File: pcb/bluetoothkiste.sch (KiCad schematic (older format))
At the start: 17 parts, among them J1 DB9_Female, J2 Screw_Terminal_01x03, J3 Screw_Terminal_01x03, J4 RJ45, J5 USB_A, J6 Conn_01x04_Female, J7 Screw_Terminal_01x03, U1 L7805, U2 MAX232

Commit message: beschriftungen pcb
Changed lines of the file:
@@
 Wire Wire Line
 	3550 7050 2950 7050
+Text Label 2950 6850 0    50   ~ 0
+COMMON-RX
+Text Label 2950 6750 0    50   ~ 0
+COMMON-TX
+Text Label 2950 6550 0    50   ~ 0
+FLARM-TX
+Text Label 2950 7050 0    50   ~ 0
+FLARM-RX
 Text Label 2950 6650 0    50   ~ 0
-COMMON-RX
-Text Label 2950 6550 0    50   ~ 0
-COMMON-TX
-Text Label 2950 6750 0    50   ~ 0
-FLARM-TX
-Text Label 2950 6850 0    50   ~ 0
-FLARM-RX
+LX-TX
 Text Label 2950 6950 0    50   ~ 0
-LX-TX
-Text Label 2950 7050 0    50   ~ 0
 LX-RX
 Wire Wire Line

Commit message: dual channel
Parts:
- removed J3, J7: Screw_Terminal_01x03, TerminalBlock_MetzConnect:TerminalBlock_MetzConnect_Type059_RT06303HBWC_1x03_P3.50mm_Horizontal, symbol Connector:Screw_Terminal_01x03
- removed J5: USB_A, JS_Local:USB_A_UPRIGHT_SEGOR, symbol Connector:USB_A
- added J3: Conn_01x04_Female, Connector_PinSocket_2.54mm:PinSocket_1x04_P2.54mm_Horizontal, symbol Connector:Conn_01x04_Female
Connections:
- net labels added: FLARM-BT-RX, FLARM-BT-TX, LX-BT-RX, LX-BT-TX
- net labels removed: BT-RX, BT-TX, COMMON-RX, COMMON-TX
- wire segments 74 -> 68
- no-connect marks 11 -> 7
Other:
- note added: "+12P = Geschaltete 12V, um die Bluetooth-Module\nausschalten zu können"
- note added: "HC-06 (FLARM)"
- note added: "HC-06 (LX)"
- note removed: "+12P = Geschaltete 12V, um das Bluetooth-Modul \nausschalten zu können"
- note removed: "COMMON-TX sollte über einen Umschalter mit\nFLARM-TX bzw. LX-TX verbunden werden, \num zwischen Flarm und LX wählen zu können. \nGenauso COMMON-RX mit FLARM-/LX-RX."
- note removed: "HC-06"
- moved on the sheet: J6
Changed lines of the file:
@@
 L Connector:Conn_01x04_Female J6
 U 1 1 5C93D289
-P 7450 4950
-F 0 "J6" H 7400 5300 50  0000 L CNN
-F 1 "Conn_01x04_Female" H 7100 5200 50  0000 L CNN
-F 2 "Connector_PinSocket_2.54mm:PinSocket_1x04_P2.54mm_Horizontal" H 7450 4950 50  0001 C CNN
-F 3 "~" H 7450 4950 50  0001 C CNN
-	1    7450 4950
+P 6750 3150
+F 0 "J6" H 6700 3500 50  0000 L CNN
+F 1 "Conn_01x04_Female" H 6400 3400 50  0000 L CNN
+F 2 "Connector_PinSocket_2.54mm:PinSocket_1x04_P2.54mm_Horizontal" H 6750 3150 50  0001 C CNN
+F 3 "~" H 6750 3150 50  0001 C CNN
+	1    6750 3150
 	-1   0    0    1
 $EndComp
@@
 $EndComp
 Connection ~ 4850 4300
-Text Notes 7250 4775 0    50   ~ 0
+Text Notes 6550 2975 0    50   ~ 0
 VCC
-Text Notes 7250 4875 0    50   ~ 0
+Text Notes 6550 3075 0    50   ~ 0
 GND
-Text Notes 7250 4975 0    50   ~ 0
+Text Notes 6550 3175 0    50   ~ 0
 TX
-Text Notes 7250 5075 0    50   ~ 0
+Text Notes 6550 3275 0    50   ~ 0
 RX
-Text Notes 7150 4650 0    50   ~ 0
-HC-06
+Text Notes 6450 2850 0    50   ~ 0
+HC-06 (FLARM)
 Wire Wire Line
 	1700 5300 1400 5300
@@
 NoConn ~ 1700 5200
 Wire Wire Line
-	3550 6550 2950 6550
-Wire Wire Line
-	3550 6650 2950 6650
-Wire Wire Line
-	3550 6750 2950 6750
-Wire Wire Line
-	3550 6850 2950 6850
-Wire Wire Line
-	3550 6950 2950 6950
-Wire Wire Line
-	3550 7050 2950 7050
-Text Label 2950 6850 0    50   ~ 0
-COMMON-RX
-Text Label 2950 6750 0    50   ~ 0
-COMMON-TX
-Text Label 2950 6550 0    50   ~ 0
-FLARM-TX
-Text Label 2950 7050 0    50   ~ 0
-FLARM-RX
-Text Label 2950 6650 0    50   ~ 0
-LX-TX
-Text Label 2950 6950 0    50   ~ 0
-LX-RX
-Wire Wire Line
 	3550 5900 3250 5900
 Wire Wire Line
@@
 $EndComp
 Text Notes 2950 6350 0    50   ~ 0
-+12P = Geschaltete 12V, um das Bluetooth-Modul \nausschalten zu können
-Text Notes 2950 7500 0    50   ~ 0
-COMMON-TX sollte über einen Umschalter mit\nFLARM-TX bzw. LX-TX verbunden werden, \num zwischen Flarm und LX wählen zu können. \nGenauso COMMON-RX mit FLARM-/LX-RX.
++12P = Geschaltete 12V, um die Bluetooth-Module\nausschalten zu können
 $Comp
 L Interface_UART:MAX232 U2
@@
 	3400 5500 4850 5500
 Wire Wire Line
-	8100 5500 8100 6200
-Wire Wire Line
-	8100 6200 9550 6200
-Wire Wire Line
 	9550 6200 9550 6100
 Wire Wire Line
@@
 Wire Wire Line
 	1400 5500 3400 5500
-Text Label 10350 5000 0    50   ~ 0
-COMMON-RX
-Text Label 10350 5400 0    50   ~ 0
-COMMON-TX
-Wire Wire Line
-	8750 5000 8350 5000
-Wire Wire Line
-	8750 5400 8350 5400
-Text Label 8350 5400 0    50   ~ 0
-BT-RX
-Text Label 8350 5000 0    50   ~ 0
-BT-TX
-Wire Wire Line
-	7650 5050 7900 5050
-Wire Wire Line
-	7650 4950 7900 4950
-Text Label 7700 4950 0    50   ~ 0
-BT-TX
-Text Label 7700 5050 0    50   ~ 0
-BT-RX
+Text Label 8150 5400 0    50   ~ 0
+LX-BT-RX
+Text Label 8150 5000 0    50   ~ 0
+LX-BT-TX
+Text Label 7100 3250 0    50   ~ 0
+FLARM-BT-RX
 Connection ~ 9550 6200
 $Comp
@@
 Wire Wire Line
 	10950 4800 10950 6200
-NoConn ~ 10350 5200
-NoConn ~ 10350 5600
-NoConn ~ 8750 5600
-NoConn ~ 8750 5200
 $Comp
 L Device:C C7
@@
 Wire Wire Line
 	9550 3700 9550 3600
-$Comp
-L Connector:USB_A J5
-U 1 1 5CA5D0AD
-P 6350 4900
-F 0 "J5" H 6407 5367 50  0000 C CNN
-F 1 "USB_A" H 6407 5276 50  0000 C CNN
-F 2 "JS_Local:USB_A_UPRIGHT_SEGOR" H 6500 4850 50  0001 C CNN
-F 3 " ~" H 6500 4850 50  0001 C CNN
-	1    6350 4900
-	1    0    0    -1
-$EndComp
-Wire Wire Line
-	6250 5300 6250 5400
-Wire Wire Line
-	6250 5400 6350 5400
-Wire Wire Line
-	6650 4700 6750 4700
-Wire Wire Line
-	6750 4700 6750 4300
-Wire Wire Line
-	6350 5300 6350 5400
-Connection ~ 6350 5400
-Wire Wire Line
-	6350 5400 6350 5500
 Wire Wire Line
 	10650 4500 10950 4500
@@
 	9550 3600 10950 3600
 Wire Wire Line
-	7250 5800 7250 6450
-Wire Wire Line
 	5400 5500 5800 5500
 Wire Wire Line
@@
 Text Notes 5300 4000 0    50   ~ 0
 R-785.0-1.0 Schaltregler\n5V 1A
-Text Label 6650 5000 0    50   ~ 0
-COMMON-TX
-Text Label 6650 4900 0    50   ~ 0
-COMMON-RX
-Connection ~ 6350 5500
-Connection ~ 6750 4300
 Connection ~ 5800 4300
 Connection ~ 5800 5500
-Wire Wire Line
-	5800 5500 6350 5500
-Wire Wire Line
-	5800 4300 6750 4300
 $Comp
 L power:+12P #PWR0110
@@
 Wire Wire Line
 	4850 3900 4850 3850
-Wire Wire Line
-	6350 5500 8100 5500
-Wire Wire Line
-	6750 4300 8100 4300
-Wire Wire Line
-	7650 4750 8100 4750
-Wire Wire Line
-	8100 4750 8100 4300
-Connection ~ 8100 4300
-Wire Wire Line
-	7650 4850 8100 4850
-Wire Wire Line
-	8100 4850 8100 5500
-Connection ~ 8100 5500
-$Comp
-L Connector:Screw_Terminal_01x03 J3
-U 1 1 5CF44711
-P 3750 6650
-F 0 "J3" H 3850 6700 50  0000 L CNN
-F 1 "Screw_Terminal_01x03" H 3850 6600 50  0000 L CNN
-F 2 "TerminalBlock_MetzConnect:TerminalBlock_MetzConnect_Type059_RT06303HBWC_1x03_P3.50mm_Horizontal" H 3750 6650 50  0001 C CNN
-F 3 "~" H 3750 6650 50  0001 C CNN
-	1    3750 6650
-	1    0    0    -1
-$EndComp
-$Comp
-L Connector:Screw_Terminal_01x03 J7
-U 1 1 5CF44F19
-P 3750 6950
-F 0 "J7" H 3850 7000 50  0000 L CNN
-F 1 "Screw_Terminal_01x03" H 3850 6900 50  0000 L CNN
-F 2 "TerminalBlock_MetzConnect:TerminalBlock_MetzConnect_Type059_RT06303HBWC_1x03_P3.50mm_Horizontal" H 3750 6950 50  0001 C CNN
-F 3 "~" H 3750 6950 50  0001 C CNN
-	1    3750 6950
-	1    0    0    -1
-$EndComp
+$Comp
+L Connector:Conn_01x04_Female J3
+U 1 1 5D01F109
+P 6750 2250
+F 0 "J3" H 6700 2600 50  0000 L CNN
+F 1 "Conn_01x04_Female" H 6400 2500 50  0000 L CNN
+F 2 "Connector_PinSocket_2.54mm:PinSocket_1x04_P2.54mm_Horizontal" H 6750 2250 50  0001 C CNN
+F 3 "~" H 6750 2250 50  0001 C CNN
+	1    6750 2250
+	-1   0    0    1
+$EndComp
+Text Notes 6550 2075 0    50   ~ 0
+VCC
+Text Notes 6550 2175 0    50   ~ 0
+GND
+Text Notes 6550 2275 0    50   ~ 0
+TX
+Text Notes 6550 2375 0    50   ~ 0
+RX
+Text Notes 6450 1950 0    50   ~ 0
+HC-06 (LX)
+Text Label 7100 3150 0    50   ~ 0
+FLARM-BT-TX
+Wire Wire Line
+	6950 3150 7100 3150
+Wire Wire Line
+	6950 3250 7100 3250
+Wire Wire Line
+	6950 2350 7100 2350
+Wire Wire Line
+	6950 2250 7100 2250
+Text Label 7100 2250 0    50   ~ 0
+LX-BT-TX
+Text Label 7100 2350 0    50   ~ 0
+LX-BT-RX
+Wire Wire Line
+	6950 2050 7900 2050
+Wire Wire Line
+	7900 2050 7900 2950
+Connection ~ 7900 4300
+Wire Wire Line
+	7900 4300 8100 4300
+Connection ~ 7900 2950
+Wire Wire Line
+	7900 2950 7900 4300
+Wire Wire Line
+	6950 3050 7800 3050
+Wire Wire Line
+	7800 2150 6950 2150
+Wire Wire Line
+	6950 2950 7900 2950
+Wire Wire Line
+	7800 2150 7800 3050
+Wire Wire Line
+	7800 3050 7800 5500
+Connection ~ 7800 3050
+Wire Wire Line
+	7800 5500 7800 6200
+Wire Wire Line
+	7800 6200 9550 6200
+Connection ~ 7800 5500
+Wire Wire Line
+	8150 5400 8750 5400
+Wire Wire Line
+	8150 5000 8750 5000
+Wire Wire Line
+	8750 5200 8150 5200
+Wire Wire Line
+	8150 5600 8750 5600
+Text Label 8150 5200 0    50   ~ 0
+FLARM-BT-TX
+Text Label 8150 5600 0    50   ~ 0
+FLARM-BT-RX
+Text Label 10350 5400 0    50   ~ 0
+LX-TX
+Text Label 10350 5600 0    50   ~ 0
+FLARM-TX
+Text Label 10350 5200 0    50   ~ 0
+FLARM-RX
+Text Label 10350 5000 0    50   ~ 0
+LX-RX
+Wire Wire Line
+	5800 4300 7900 4300
+Wire Wire Line
+	5800 5500 7800 5500
 $EndSCHEMATC

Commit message: bugs in schematic
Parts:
- added J5: USB_A, symbol Connector:USB_A
- added JP1: Jumper, symbol Device:Jumper
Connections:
- net +12P: now also JP1.2
- net +12V: now also J4.7, J4.8, JP1.1; no longer J4.1, J4.2
- net +5V: now also J5.1 (VBUS)
- net FLARM-RX: now also J4.3; no longer J4.6
- net FLARM-TX: now also J4.4; no longer J4.5
- net GND: now also J4.1, J4.2, J4.5, J5.4 (GND), J5.5 (Shield); no longer J4.4, J4.7, J4.8
- net LX-RX: now also J1.3; no longer J1.2
- net LX-TX: now also J1.2; no longer J1.3
- no-connect marks 7 -> 9
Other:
- note added: "+12P = Stromversorgung Bluetooth-Module (intern abgesichert)\n+12V = Stromversorgung FLARM (intern nicht abgesichert)"
- note added: "Jumper zum Verbinden der Stromversorgung \nder Bluetooth-Module und des FLARM. \nFalls man nicht getrennt ein- und ausschalten\nmöchte kann man diesen Jumper setzen."
- note removed: "+12P = Geschaltete 12V, um die Bluetooth-Module\nausschalten zu können"
- moved on the sheet: J4
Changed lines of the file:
@@
 L Connector:RJ45 J4
 U 1 1 5C93DA28
-P 4100 4850
-F 0 "J4" H 3770 4854 50  0000 R CNN
-F 1 "RJ45" H 3770 4945 50  0000 R CNN
-F 2 "JS_Local:RJ45_SEGOR" V 4100 4875 50  0001 C CNN
-F 3 "~" V 4100 4875 50  0001 C CNN
-	1    4100 4850
-	-1   0    0    1
+P 3300 4950
+F 0 "J4" H 2970 4954 50  0000 R CNN
+F 1 "RJ45" H 2970 5045 50  0000 R CNN
+F 2 "JS_Local:RJ45_SEGOR" V 3300 4975 50  0001 C CNN
+F 3 "~" V 3300 4975 50  0001 C CNN
+	1    3300 4950
+	1    0    0    -1
 $EndComp
 $Comp
@@
 	1700 5300 1400 5300
 Wire Wire Line
-	3700 5250 3400 5250
-Wire Wire Line
-	3700 5150 3400 5150
-Wire Wire Line
-	3400 5150 3400 5250
-Wire Wire Line
-	3700 4850 3400 4850
-Wire Wire Line
-	3400 4850 3400 5150
-Connection ~ 3400 5150
+	3900 5150 3900 5250
+Wire Wire Line
+	3900 4850 3900 5150
+Connection ~ 3900 5150
 NoConn ~ 3700 4750
-Wire Wire Line
-	3700 4650 3600 4650
-Wire Wire Line
-	3700 4550 3600 4550
-Wire Wire Line
-	3600 4550 3600 4650
-Connection ~ 3600 4650
-Wire Wire Line
-	3600 4650 3400 4650
-Wire Wire Line
-	3700 4950 2750 4950
-Text Label 2750 4950 0    50   ~ 0
+Text Label 4150 4950 0    50   ~ 0
 FLARM-TX
-Wire Wire Line
-	3700 5050 2750 5050
-Text Label 2750 5050 0    50   ~ 0
+Text Label 4150 5050 0    50   ~ 0
 FLARM-RX
 Wire Wire Line
 	750  4900 1700 4900
-Text Label 750  4900 0    50   ~ 0
+Text Label 750  4700 0    50   ~ 0
 LX-TX
 NoConn ~ 1700 4500
@@
 $EndComp
 Text Notes 2950 6350 0    50   ~ 0
-+12P = Geschaltete 12V, um die Bluetooth-Module\nausschalten zu können
++12P = Stromversorgung Bluetooth-Module (intern abgesichert)\n+12V = Stromversorgung FLARM (intern nicht abgesichert)
 $Comp
 L Interface_UART:MAX232 U2
@@
 	4850 5500 5400 5500
 Wire Wire Line
-	3400 5250 3400 5500
-Connection ~ 3400 5250
-Connection ~ 3400 5500
-Wire Wire Line
-	3400 5500 4850 5500
+	3900 5250 3900 5500
+Connection ~ 3900 5250
 Wire Wire Line
 	9550 6200 9550 6100
@@
 $EndComp
 Wire Wire Line
-	4550 4300 3400 4300
-Wire Wire Line
-	3400 4650 3400 4300
-Connection ~ 3400 4300
-Wire Wire Line
-	3400 4300 750  4300
+	4550 4300 3900 4300
+Wire Wire Line
+	3900 4650 3900 4550
 $Comp
 L power:+12V #PWR0106
 U 1 1 5CA1F7A5
-P 4550 4300
-F 0 "#PWR0106" H 4550 4150 50  0001 C CNN
-F 1 "+12V" H 4565 4473 50  0000 C CNN
-F 2 "" H 4550 4300 50  0001 C CNN
-F 3 "" H 4550 4300 50  0001 C CNN
-	1    4550 4300
+P 4400 2300
+F 0 "#PWR0106" H 4400 2150 50  0001 C CNN
+F 1 "+12V" H 4415 2473 50  0000 C CNN
+F 2 "" H 4400 2300 50  0001 C CNN
+F 3 "" H 4400 2300 50  0001 C CNN
+	1    4400 2300
 	1    0    0    -1
 $EndComp
@@
 	1    0    0    -1
 $EndComp
-Text Label 750  4700 0    50   ~ 0
+Text Label 750  4900 0    50   ~ 0
 LX-RX
 Wire Wire Line
@@
 	1400 5300 1400 5500
 Connection ~ 1400 5500
-Wire Wire Line
-	1400 5500 3400 5500
 Text Label 8150 5400 0    50   ~ 0
 LX-BT-RX
@@
 L power:+12P #PWR0110
 U 1 1 5C941CC9
-P 4850 3850
-F 0 "#PWR0110" H 4850 3700 50  0001 C CNN
-F 1 "+12P" H 4865 4023 50  0000 C CNN
-F 2 "" H 4850 3850 50  0001 C CNN
-F 3 "" H 4850 3850 50  0001 C CNN
-	1    4850 3850
+P 5000 2300
+F 0 "#PWR0110" H 5000 2150 50  0001 C CNN
+F 1 "+12P" H 5015 2473 50  0000 C CNN
+F 2 "" H 5000 2300 50  0001 C CNN
+F 3 "" H 5000 2300 50  0001 C CNN
+	1    5000 2300
 	1    0    0    -1
 $EndComp
@@
 Wire Wire Line
 	4850 4200 4850 4300
-Wire Wire Line
-	4850 3900 4850 3850
 $Comp
 L Connector:Conn_01x04_Female J3
@@
 LX-RX
 Wire Wire Line
-	5800 4300 7900 4300
-Wire Wire Line
-	5800 5500 7800 5500
+	5800 4300 7250 4300
+Wire Wire Line
+	5800 5500 6600 5500
+$Comp
+L Connector:USB_A J5
+U 1 1 5D2F7C66
+P 6700 4850
+F 0 "J5" H 6757 5317 50  0000 C CNN
+F 1 "USB_A" H 6757 5226 50  0000 C CNN
+F 2 "" H 6850 4800 50  0001 C CNN
+F 3 " ~" H 6850 4800 50  0001 C CNN
+	1    6700 4850
+	1    0    0    -1
+$EndComp
+NoConn ~ 7000 4850
+NoConn ~ 7000 4950
+Wire Wire Line
+	7000 4650 7250 4650
+Wire Wire Line
+	7250 4650 7250 4300
+Connection ~ 7250 4300
+Wire Wire Line
+	7250 4300 7900 4300
+Wire Wire Line
+	6700 5250 6700 5500
+Connection ~ 6700 5500
+Wire Wire Line
+	6700 5500 7800 5500
+Wire Wire Line
+	6600 5250 6600 5500
+Connection ~ 6600 5500
+Wire Wire Line
+	6600 5500 6700 5500
+Connection ~ 3900 5500
+Wire Wire Line
+	3900 5500 4850 5500
+Wire Wire Line
+	1400 5500 3900 5500
+Connection ~ 3900 4300
+Wire Wire Line
+	750  4300 3900 4300
+Wire Wire Line
+	3900 5150 3700 5150
+Wire Wire Line
+	3700 5250 3900 5250
+Wire Wire Line
+	3900 4850 3700 4850
+Wire Wire Line
+	3900 4650 3700 4650
+Wire Wire Line
+	3700 4550 3900 4550
+Connection ~ 3900 4550
+Wire Wire Line
+	3900 4550 3900 4300
+Wire Wire Line
+	3700 4950 4150 4950
+Wire Wire Line
+	3700 5050 4150 5050
+$Comp
+L Device:Jumper JP1
+U 1 1 5D378146
+P 4700 2700
+F 0 "JP1" H 4700 2964 50  0000 C CNN
+F 1 "Jumper" H 4700 2873 50  0000 C CNN
+F 2 "" H 4700 2700 50  0001 C CNN
+F 3 "~" H 4700 2700 50  0001 C CNN
+	1    4700 2700
+	1    0    0    -1
+$EndComp
+Wire Wire Line
+	5000 2700 5000 3400
+Wire Wire Line
+	5000 3400 4850 3400
+Wire Wire Line
+	4400 2300 4400 2700
+Wire Wire Line
+	4850 3400 4850 3900
+Wire Wire Line
+	5000 2700 5000 2300
+Connection ~ 5000 2700
+Wire Wire Line
+	4400 2700 4400 3400
+Wire Wire Line
+	4400 3400 4550 3400
+Wire Wire Line
+	4550 3400 4550 4300
+Connection ~ 4400 2700
+Text Notes 2450 2900 0    50   ~ 0
+Jumper zum Verbinden der  Stromversorgung \nder Bluetooth-Module und des FLARM. \nFalls man nicht getrennt ein- und ausschalten\nmöchte kann man diesen Jumper setzen.
 $EndSCHEMATC

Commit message: layout updated
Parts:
- J2: footprint TerminalBlock_MetzConnect:TerminalBlock_MetzConnect_Type059_RT06303HBWC_1x03_P3.50mm_Horizontal -> TerminalBlock_MetzConnect:TerminalBlock_MetzConnect_Type055_RT01503HDWU_1x03_P5.00mm_Horizontal
- J5: footprint (none) -> JS_Local:USB_A_UPRIGHT_SEGOR
- JP1: footprint (none) -> Connector_PinHeader_2.54mm:PinHeader_1x02_P2.54mm_Vertical
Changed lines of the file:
@@
 F 0 "J2" H 3850 6050 50  0000 L CNN
 F 1 "Screw_Terminal_01x03" H 3850 5950 50  0000 L CNN
-F 2 "TerminalBlock_MetzConnect:TerminalBlock_MetzConnect_Type059_RT06303HBWC_1x03_P3.50mm_Horizontal" H 3750 6000 50  0001 C CNN
+F 2 "TerminalBlock_MetzConnect:TerminalBlock_MetzConnect_Type055_RT01503HDWU_1x03_P5.00mm_Horizontal" H 3750 6000 50  0001 C CNN
 F 3 "~" H 3750 6000 50  0001 C CNN
 	1    3750 6000
@@
 F 0 "J5" H 6757 5317 50  0000 C CNN
 F 1 "USB_A" H 6757 5226 50  0000 C CNN
-F 2 "" H 6850 4800 50  0001 C CNN
+F 2 "JS_Local:USB_A_UPRIGHT_SEGOR" H 6850 4800 50  0001 C CNN
 F 3 " ~" H 6850 4800 50  0001 C CNN
 	1    6700 4850
@@
 F 0 "JP1" H 4700 2964 50  0000 C CNN
 F 1 "Jumper" H 4700 2873 50  0000 C CNN
-F 2 "" H 4700 2700 50  0001 C CNN
+F 2 "Connector_PinHeader_2.54mm:PinHeader_1x02_P2.54mm_Vertical" H 4700 2700 50  0001 C CNN
 F 3 "~" H 4700 2700 50  0001 C CNN
 	1    4700 2700

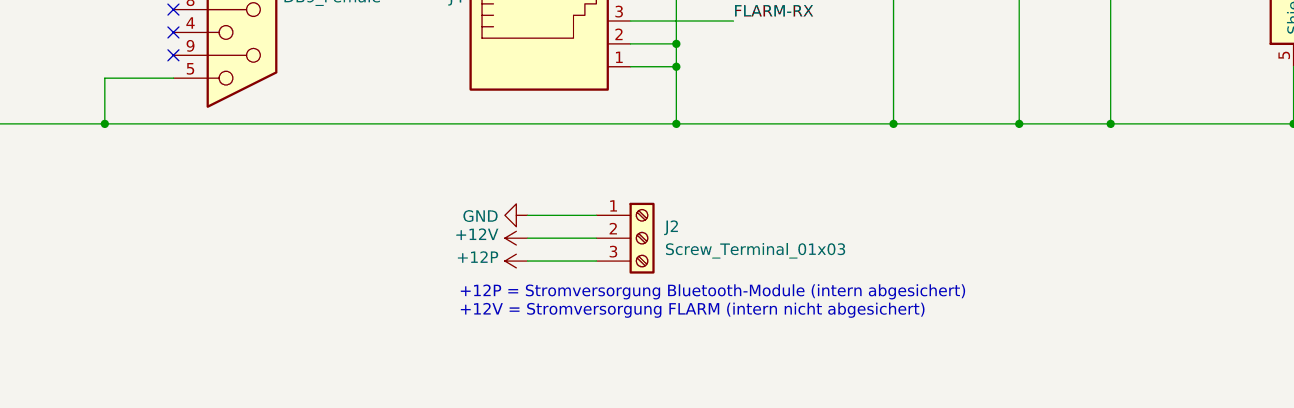
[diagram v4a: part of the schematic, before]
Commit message: dioden verpolungsschutz
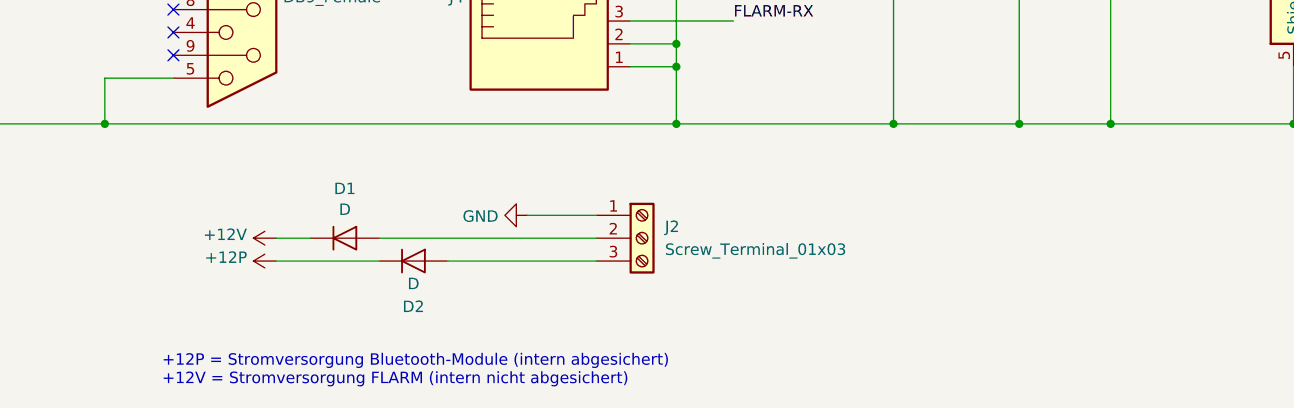
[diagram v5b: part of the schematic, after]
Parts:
- added D1, D2: D, Diode_THT:D_A-405_P7.62mm_Horizontal, symbol Device:D
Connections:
- net +12P: now also D2.1 (K); no longer J2.3 (Pin_3)
- net +12V: now also D1.1 (K); no longer J2.2 (Pin_2)
- new net: D1.2 (A), J2.2 (Pin_2)
- new net: D2.2 (A), J2.3 (Pin_3)
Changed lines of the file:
@@
 Wire Wire Line
 	3550 5900 3250 5900
-Wire Wire Line
-	3550 6000 3250 6000
-Wire Wire Line
-	3550 6100 3250 6100
 $Comp
 L power:GND #PWR0102
@@
 L power:+12V #PWR0103
 U 1 1 5C95BA3F
-P 3250 6000
-F 0 "#PWR0103" H 3250 5850 50  0001 C CNN
-F 1 "+12V" V 3265 6128 50  0000 L CNN
-F 2 "" H 3250 6000 50  0001 C CNN
-F 3 "" H 3250 6000 50  0001 C CNN
-	1    3250 6000
+P 2150 6000
+F 0 "#PWR0103" H 2150 5850 50  0001 C CNN
+F 1 "+12V" V 2165 6128 50  0000 L CNN
+F 2 "" H 2150 6000 50  0001 C CNN
+F 3 "" H 2150 6000 50  0001 C CNN
+	1    2150 6000
 	0    -1   -1   0
 $EndComp
@@
 L power:+12P #PWR0104
 U 1 1 5C95BA9E
-P 3250 6100
-F 0 "#PWR0104" H 3250 5950 50  0001 C CNN
-F 1 "+12P" V 3265 6227 50  0000 L CNN
-F 2 "" H 3250 6100 50  0001 C CNN
-F 3 "" H 3250 6100 50  0001 C CNN
-	1    3250 6100
+P 2150 6100
+F 0 "#PWR0104" H 2150 5950 50  0001 C CNN
+F 1 "+12P" V 2165 6227 50  0000 L CNN
+F 2 "" H 2150 6100 50  0001 C CNN
+F 3 "" H 2150 6100 50  0001 C CNN
+	1    2150 6100
 	0    -1   -1   0
 $EndComp
-Text Notes 2950 6350 0    50   ~ 0
+Text Notes 1650 6650 0    50   ~ 0
 +12P = Stromversorgung Bluetooth-Module (intern abgesichert)\n+12V = Stromversorgung FLARM (intern nicht abgesichert)
 $Comp
@@
 Text Notes 2450 2900 0    50   ~ 0
 Jumper zum Verbinden der  Stromversorgung \nder Bluetooth-Module und des FLARM. \nFalls man nicht getrennt ein- und ausschalten\nmöchte kann man diesen Jumper setzen.
+$Comp
+L Device:D D2
+U 1 1 5D40CFDE
+P 2750 6100
+F 0 "D2" H 2750 5900 50  0000 C CNN
+F 1 "D" H 2750 6000 50  0000 C CNN
+F 2 "Diode_THT:D_A-405_P7.62mm_Horizontal" H 2750 6100 50  0001 C CNN
+F 3 "~" H 2750 6100 50  0001 C CNN
+	1    2750 6100
+	1    0    0    -1
+$EndComp
+$Comp
+L Device:D D1
+U 1 1 5D41055A
+P 2450 6000
+F 0 "D1" H 2450 6216 50  0000 C CNN
+F 1 "D" H 2450 6125 50  0000 C CNN
+F 2 "Diode_THT:D_A-405_P7.62mm_Horizontal" H 2450 6000 50  0001 C CNN
+F 3 "~" H 2450 6000 50  0001 C CNN
+	1    2450 6000
+	1    0    0    -1
+$EndComp
+Wire Wire Line
+	2600 6000 3550 6000
+Wire Wire Line
+	2300 6000 2150 6000
+Wire Wire Line
+	2150 6100 2600 6100
+Wire Wire Line
+	2900 6100 3550 6100
 $EndSCHEMATC
